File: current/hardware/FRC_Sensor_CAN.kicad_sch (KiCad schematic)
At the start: 0 parts

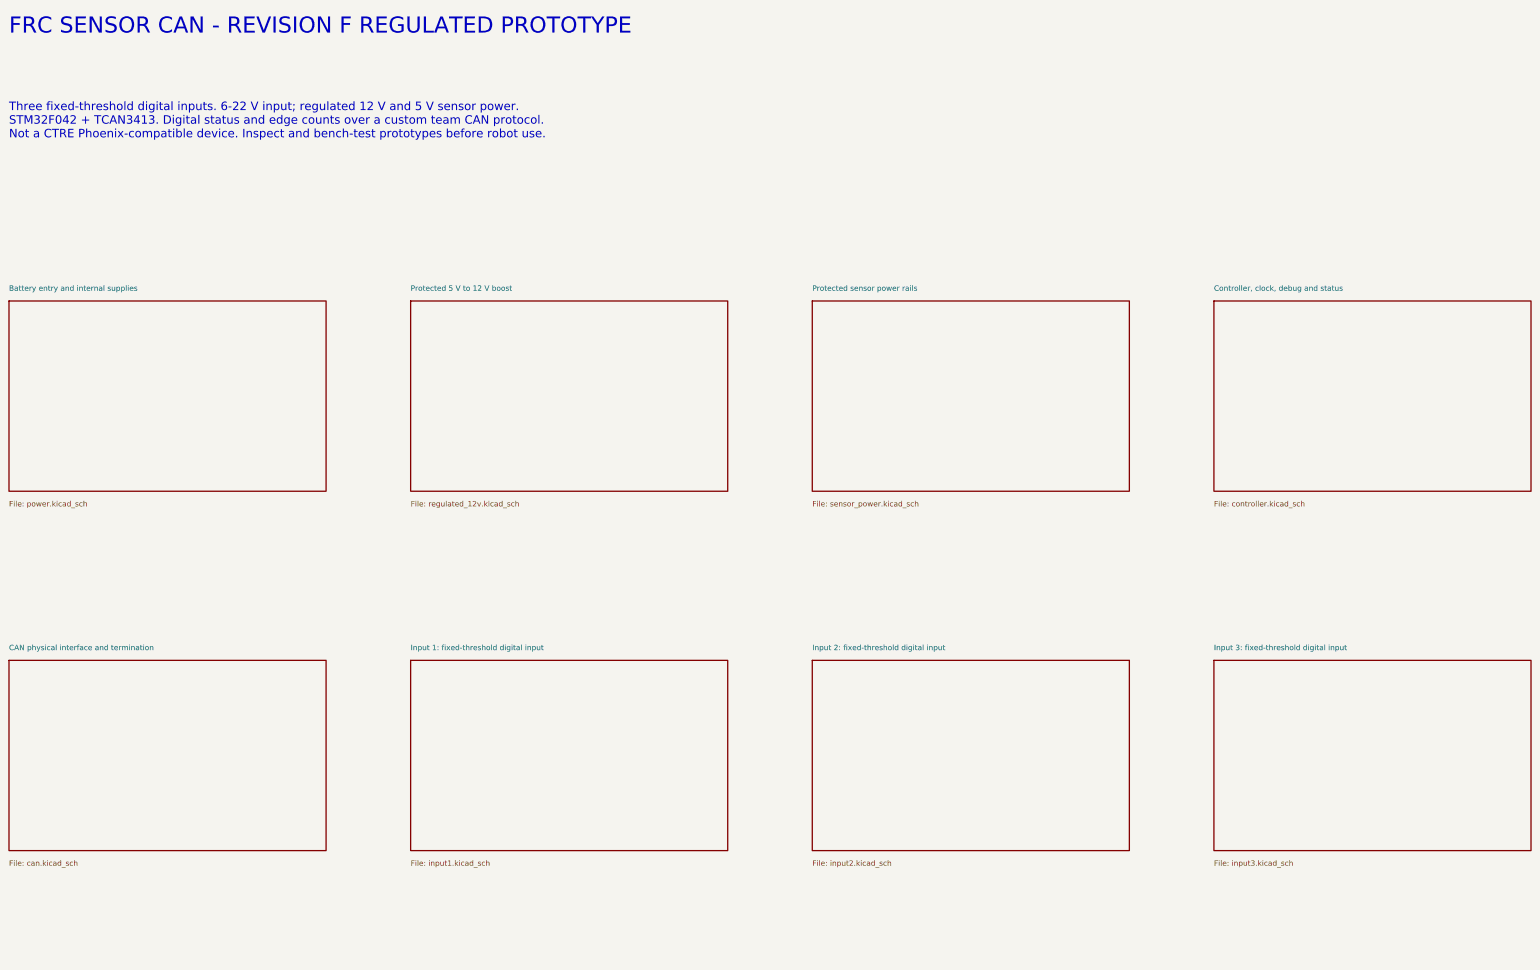
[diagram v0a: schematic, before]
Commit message: Rev G: protect sensor power and verify startup and fault recovery
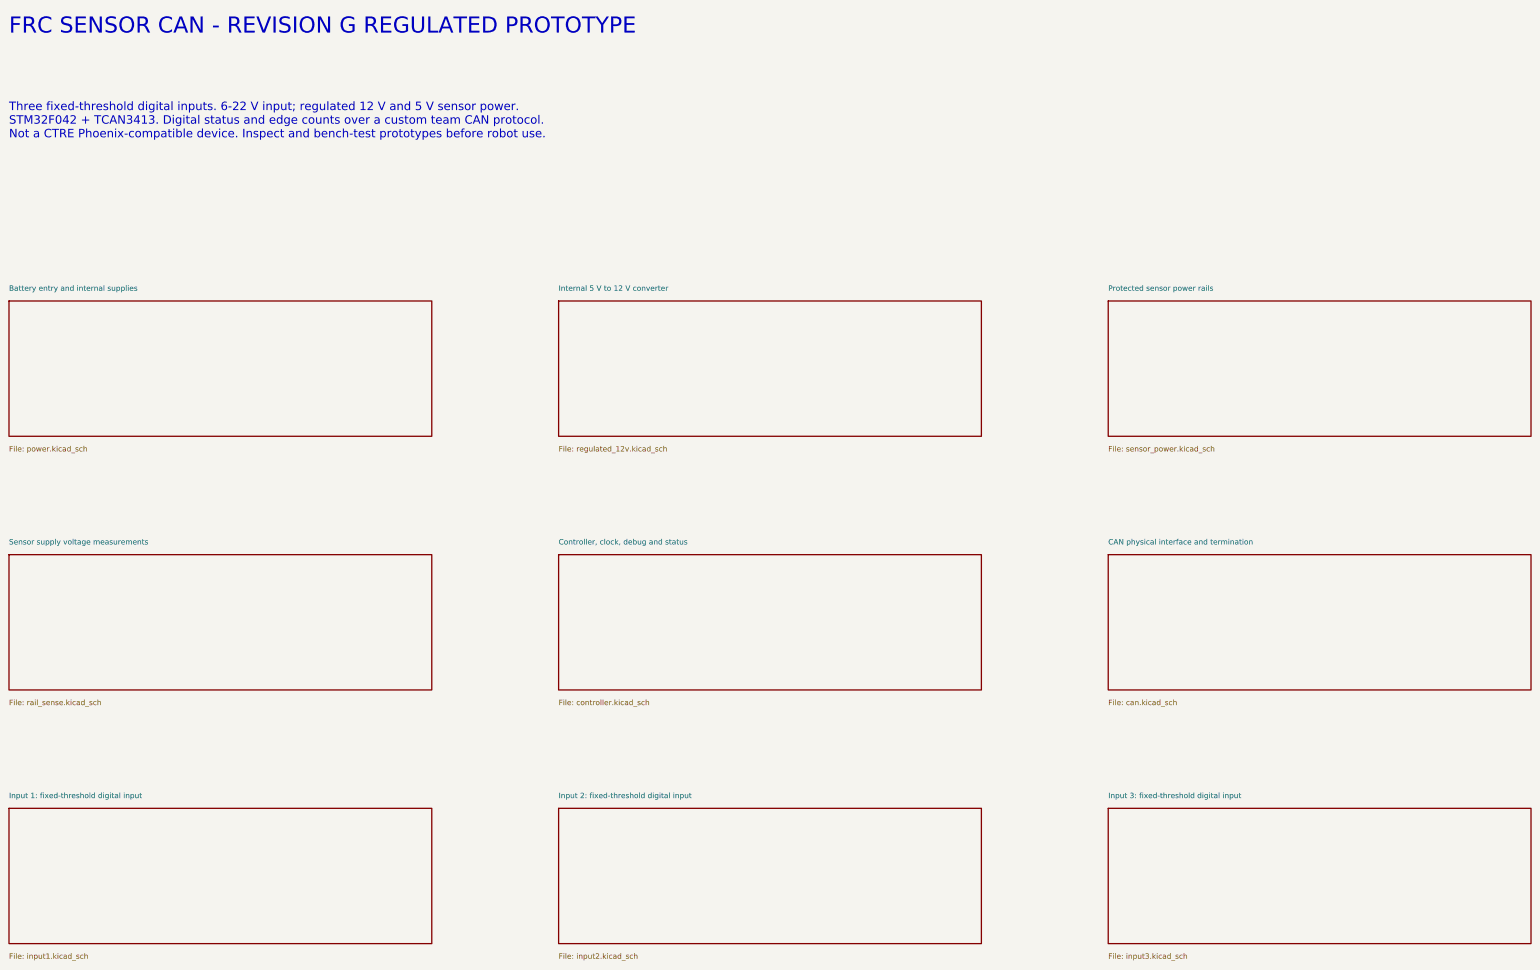
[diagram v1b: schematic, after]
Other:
- sheet Protected 5 V to 12 V boost renamed Internal 5 V to 12 V converter
- added sheet Sensor supply voltage measurements (rail_sense.kicad_sch)
- note added: "FRC SENSOR CAN - REVISION G REGULATED PROTOTYPE"
- note removed: "FRC SENSOR CAN - REVISION F REGULATED PROTOTYPE"

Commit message: Add Rev H RGB status and low-cost programming header
Keep sensor power and inputs unchanged. Add buffered ARGB status, nonblocking timer/DMA firmware, ordinary hand-fitted SWD header, and updated CAD/BOM/docs. Native and focused firmware checks pass. Explicitly record the canceled full power rerun as incomplete; retain full-release gates and preserve all historical packages.
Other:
- note added: "FRC SENSOR CAN - REVISION H REGULATED PROTOTYPE"
- note removed: "FRC SENSOR CAN - REVISION G REGULATED PROTOTYPE"
